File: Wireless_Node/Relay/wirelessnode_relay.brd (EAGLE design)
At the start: 50 x 42 mm, 45 parts, among them CON2 ZL321-4P, IC1 LNK304, IC2 STM8L101F2, IC3 MCP1703, T1 VO3063-X007T, T2 BTA16

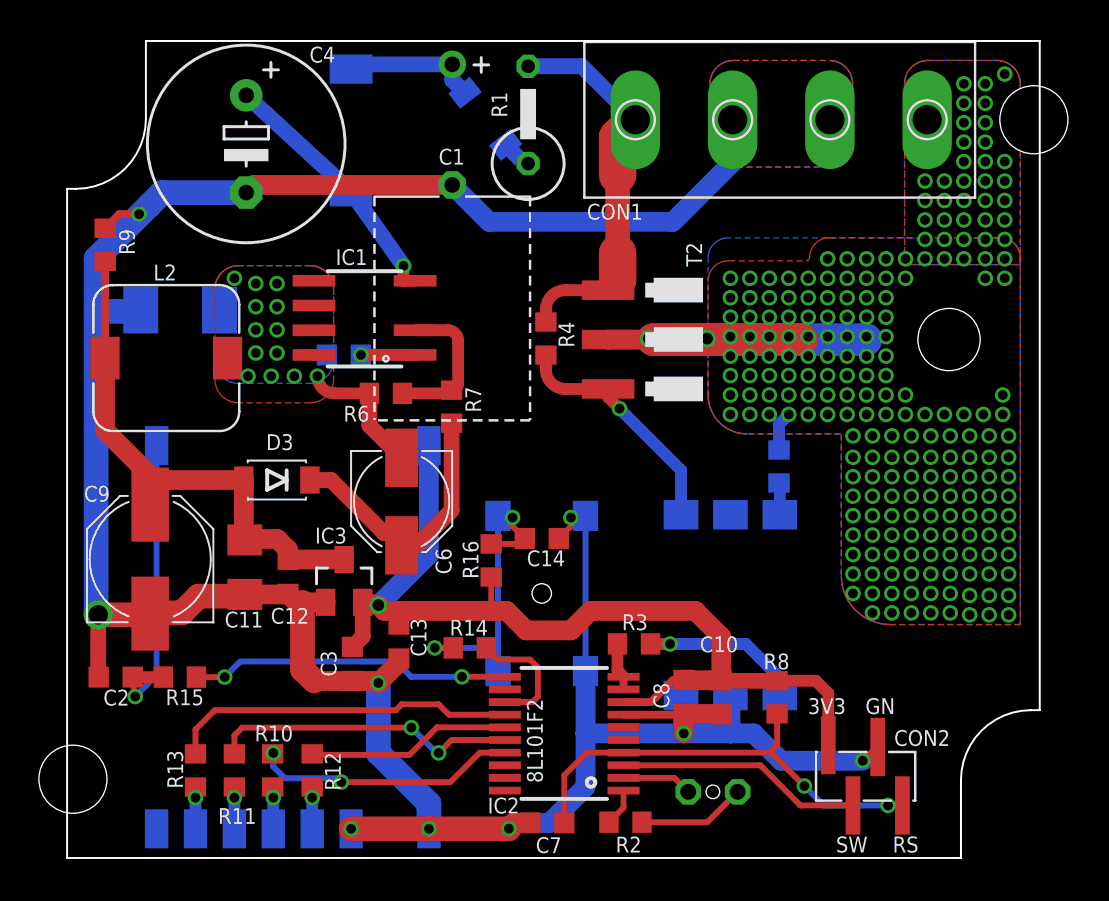
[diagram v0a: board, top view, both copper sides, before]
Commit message: Split project into Relay and Triac based wireless node
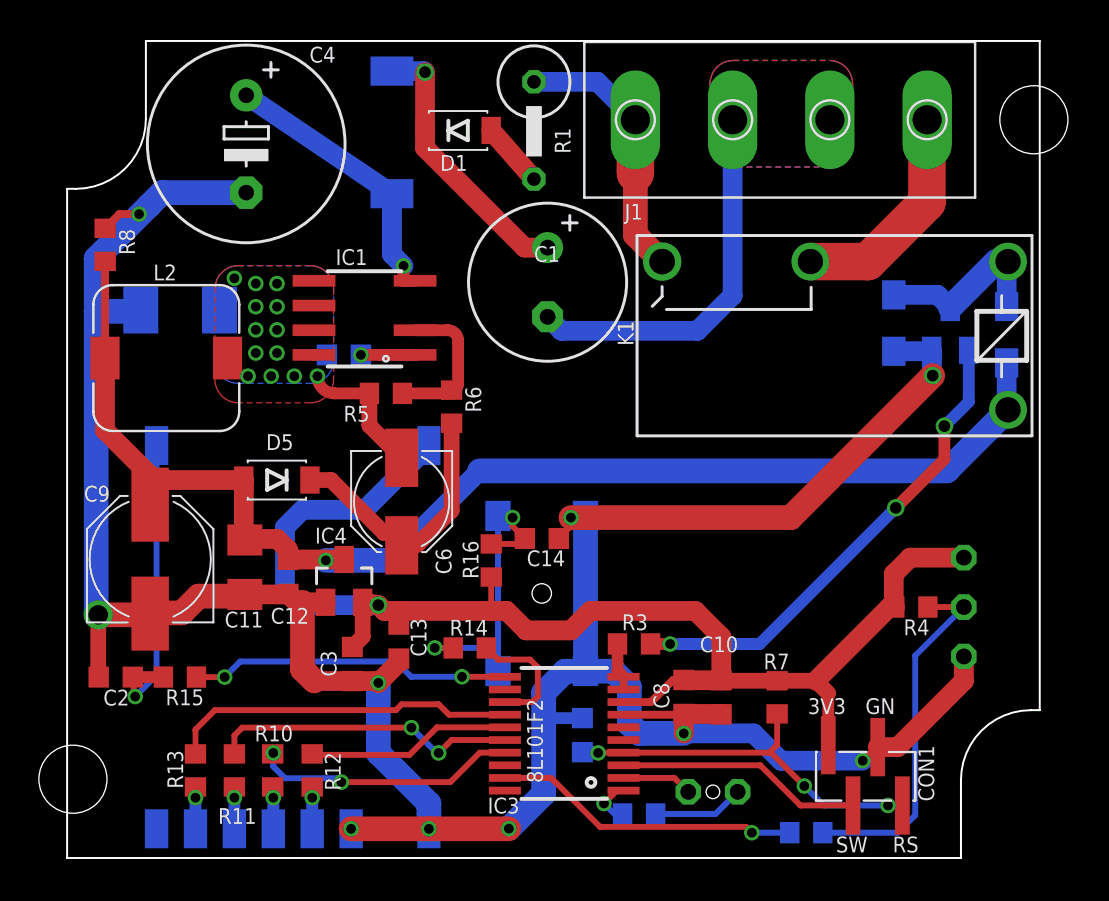
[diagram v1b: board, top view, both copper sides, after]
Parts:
- removed CON2: ZL321-4P, comp_wirelessnode:CON_1X4_1.27_SMD
- removed T2: BTA16, comp_wirelessnode:TO220_SMD
- added D4: 1A/400V, comp_wirelessnode:DO214-AC
- added D5: 1A/400V, comp_wirelessnode:SOD-123F
- added IC4: MCP1703, linear:SOT23
- added J1: (no value), CarReceiver:TERMINAL_BLOCK_4
- added K1: (no value), comp_wirelessnode:G5Q-1A4-EU
- C1: device comp_wirelessnode:CAP_8X11.5_AIR -> comp_wirelessnode:E3.5-8
- CON1: value (none) -> ZL321-4P; device CarReceiver:TERMINAL_BLOCK_4 -> comp_wirelessnode:CON_1X4_1.27_SMD
- D2: value 1A/400V -> BAS16HT1G; device comp_wirelessnode:DO214-AC -> diode:SOD323-W
- D3: value 1A/400V -> BAS16HT1G; device comp_wirelessnode:SOD-123F -> diode:SOD323-W
- IC2: value STM8L101F2 -> DS18B20; device comp_wirelessnode:TSSOP20 -> 1wire:TO92-
- IC3: value MCP1703 -> STM8L101F2; device linear:SOT23 -> comp_wirelessnode:TSSOP20
- R3: value 220 -> 2.2k
- R4: value 360 -> 4.7k
- R5: value 360 -> 2k
- R6: value 2k -> 12k
- R7: value 8.6K -> 10k
- R8: value 10k -> 3.3k
- R9: value 3.3k -> 47
- T1: value VO3063-X007T -> BC817; device optocoupler:DIL6-SMD -> transistor:SOT23-BEC
- moved R9 47.0 mm to (38.0, 2.30), flipped to the bottom, turned to 180 degrees
- moved D2 42.5 mm to (48.3, 27.9), turned to 90 degrees
- moved R8 41.6 mm to (1.96, 32.5), turned to 270 degrees
- moved CON1 34.0 mm to (40.4, 5.20), turned to 0 degrees
- moved D3 32.7 mm to (42.5, 28.5), flipped to the bottom, turned to 270 degrees
- moved R4 23.3 mm to (43.4, 13.9), turned to 180 degrees
- moved R7 22.4 mm to (36.5, 9.26), turned to 90 degrees
- moved IC2 21.4 mm to (46.1, 13.9), flipped to the bottom
- moved R5 20.6 mm to (16.4, 24.9), flipped to the top, turned to 0 degrees
- moved T1 18.1 mm to (45.4, 28.2)
- moved IC3 13.4 mm to (25.6, 8.04), turned to 90 degrees
- moved C1 7.00 mm to (24.7, 30.6)
- moved C7 4.85 mm to (26.5, 7.32), flipped to the bottom, turned to 90 degrees
- moved R1 4.21 mm to (24.0, 40.9), turned to 270 degrees
- moved R6 3.45 mm to (19.8, 24.2), turned to 270 degrees
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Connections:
- removed net +9.2V: C11.1, C12.1, C9.+, D3.2, IC3.3, L2.P$2, R9.2
- removed net LIGHT_ON: IC2.10, IC2.9, R3.1
- removed net N$12: D1.2, R1.1
- new net +12V: C11.1, C12.1, C9.+, D2.C, D5.2, IC4.3, K1.1, L2.P$2, R8.2
- new net DQ: IC2.2, R4.1, R9.2
- new net LOAD_ON: IC3.10, IC3.9, R3.1
- new net N$18: IC3.19, R9.1
- net +3V3: now also CON1.1, IC2.3, IC3.8, IC4.2, R4.2, R7.2; no longer CON2.1, IC2.8, IC3.2, R8.2
- net GND: now also D3.A, D4.A, IC2.1, IC3.7, IC4.1, J1.2, J1.3, R8.1, T1.E; no longer CON1.2, CON2.3, D2.A, IC2.7, IC3.1, R9.1, T1.2
- net L: now also J1.4, K1.3, R1.1; no longer CON1.4, R1.2, R4.1, T2.1
- net LED_TX_ERR1: now also IC3.1; no longer IC2.1
- net LED_TX_ERR2: now also IC3.2; no longer IC2.2
- net LOAD: now also J1.1, K1.2; no longer CON1.1, R5.2, T2.2
- net N$11: now also T1.B; no longer T1.1
- net N$13: now also IC3.15; no longer IC2.15
- net N$14: now also IC3.16; no longer IC2.16
- net N$15: now also IC3.17; no longer IC2.17
- net N$16: now also IC3.11; no longer IC2.11
- net N$17: now also IC3.13; no longer IC2.13
- net N$3: now also D5.1, R6.2; no longer D3.1, R7.2
- net N$4: now also R5.2, R6.1; no longer R6.2, R7.1
- net N$6: now also D4.C, R5.1; no longer D2.C, R6.1
- net N$7: now also D1.2, R1.2; no longer R5.1, T1.6
- net N$8: now also D2.A, D3.C, K1.5, T1.C; no longer R4.2, T1.4, T2.3
- net N$9: now also IC3.14; no longer IC2.14
- net RST: now also CON1.4, IC3.4, R7.1; no longer CON2.4, IC2.4, R8.1
- net SWIM: now also CON1.2, IC3.3; no longer CON2.2, IC2.3
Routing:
- net +12V: track 0.00 -> 68.0 mm, vias 0 -> 1
- net +9.2V: track 27.2 -> 0.00 mm
- net GND: track 149.7 -> 172.7 mm, vias 9 -> 10
- net +3V3: track 50.4 -> 69.9 mm
- net DQ: track 0.00 -> 18.7 mm
- net N$11: track 8.27 -> 25.2 mm, vias 1 -> 3
- net N$18: track 0.00 -> 15.8 mm, vias 0 -> 1
- net LOAD: track 23.7 -> 11.5 mm, vias 218 -> 0
- net N$10: track 7.03 -> 14.0 mm, vias 0 -> 1
- net L: track 20.5 -> 13.9 mm
- net RST: track 23.7 -> 19.8 mm, vias 2 -> 3
- net N$8: track 12.4 -> 9.46 mm, vias 1 -> 0
- net LOAD_ON: track 0.00 -> 2.47 mm
- net LIGHT_ON: track 2.47 -> 0.00 mm
- net N$7: track 1.65 -> 3.33 mm
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- removed copper zone on layer 1, net LOAD
- removed copper zone on layer 16, net LOAD

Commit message: Ready for production
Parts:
- removed D5: 1A/400V, comp_wirelessnode:SOD-123F
- removed J1: (no value), CarReceiver:TERMINAL_BLOCK_4
- added B1: B05S, rectifier:MBS
- added C15: (no value), resistor:C1812
- added CON2: ZL321-4P, comp_wirelessnode:CON_1X4_1.27_SMD
- added R17: (no value), resistor:R2010
- C4: value 4.7u/400V -> 2.2u/400V; device comp_RFSwitch_v3:E5-10,5 -> comp_wirelessnode:E3.5-8
- CON1: value ZL321-4P -> (none); device comp_wirelessnode:CON_1X4_1.27_SMD -> CarReceiver:TERMINAL_BLOCK_4
- D1: value 1A/400V -> BAS16HT1G; device comp_wirelessnode:SOD-123F -> diode:SOD323-W
- D3: value BAS16HT1G -> 1A/400V; device diode:SOD323-W -> comp_wirelessnode:DO214-AC
- D4: device comp_wirelessnode:DO214-AC -> comp_wirelessnode:SOD-123F
- moved D3 36.7 mm to (5.81, 29.2), turned to 0 degrees
- moved CON1 34.0 mm to (36.6, 39.0), turned to 270 degrees
- moved D1 30.2 mm to (48.3, 27.6), flipped to the bottom, turned to 90 degrees
- moved D4 10.1 mm to (10.8, 20.4), flipped to the top, turned to 180 degrees
- moved R1 9.46 mm to (26.9, 31.9), turned to 180 degrees
- moved C1 9.36 mm to (20.0, 38.7)
- moved R4 7.26 mm to (36.3, 12.4)
- moved D2 5.61 mm to (42.7, 28.2), turned to 270 degrees
- moved L1 2.55 mm to (14.2, 38.4)
- moved C4 1.35 mm to (8.30, 38.7)
- moved T1 0.36 mm to (45.6, 27.9)
- moved K1 0.30 mm to (49.6, 32.7)
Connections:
- removed net LOAD: J1.1, K1.2
- new net N: B1.AC2, CON1.3
- new net N$12: C15.2, R17.2
- new net SW1: C15.1, CON1.1, K1.2
- new net SW2: CON1.2, K1.3, R17.1
- net +12V: now also D1.C, D4.2; no longer D2.C, D5.2
- net +3V3: now also CON2.1; no longer CON1.1
- net GND: now also B1.-, CON2.3, D2.A; no longer CON1.3, D4.A, J1.2, J1.3
- net L: now also CON1.4; no longer J1.4, K1.3
- net N$10: now also B1.+; no longer D1.1
- net N$3: now also D4.1; no longer D5.1
- net N$6: now also D3.C; no longer D4.C
- net N$7: now also B1.AC1; no longer D1.2
- net N$8: now also D1.A, D2.C; no longer D2.A, D3.C
- net RST: now also CON2.4; no longer CON1.4
- net SWIM: now also CON2.2; no longer CON1.2
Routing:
- net SW2: track 0.00 -> 17.2 mm
- net SW1: track 0.00 -> 15.2 mm
- net N: track 0.00 -> 13.1 mm
- net LOAD: track 11.5 -> 0.00 mm
- net GND: track 172.7 -> 184.1 mm, vias 10 -> 12
- net DQ: track 18.7 -> 26.2 mm, vias 0 -> 1
- net L: track 13.9 -> 8.01 mm
- net +3V3: track 69.9 -> 75.1 mm
- net N$10: track 14.0 -> 9.85 mm, vias 1 -> 0
- net N$12: track 0.00 -> 2.17 mm
- net N$8: track 9.46 -> 8.23 mm
- net N$7: track 3.33 -> 4.11 mm
- net N$11: track 25.2 -> 25.8 mm
- removed copper zone on layer 1, net GND
- removed copper zone on layer 16, net GND
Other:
- outline, holes or cut-outs redrawn
- board text added: "SW1"
- board text added: "SW2"
- board text added: "Wifi node R1-R1-T1 v1.0"
- board text removed: "LOAD"
